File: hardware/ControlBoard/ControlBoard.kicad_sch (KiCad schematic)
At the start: 140 parts, among them J1 Lamp 1 Out, J10 CAN, J11 USB_B_Micro, J12 Conn_01x02, J13 AVAILABLE GPIO, J14 MOTOR_CTRL1, J15 MOTOR_CTRL2, J2 ESTOP1, J3 ESTOP2, J4 Lamp 3 Out, J5 Lamp 2 Out, J6 Lamp 4 Out, J7 PWR_IN, J8 USB_B_Micro, J9 UART BACKUP, Q1 2N7002, Q2 2N7002, Q3 2N7002, Q4 2N7002, Q5 SS8050-G, Q6 SS8050-G, SW1 SW_Push, SW2 SW_Push, U1 CP2102N-A02-GQFN28, U10 TXB0106PWR, U2 Lora_Module, U3 AZ1117IH-5.0TRG1, U4 LD1086DT33TR, U5 ESP32-S3-WROOM-1U, U6 74LVC1G97W6-7, U7 SN65HVD232, U8 SN74LVC1GU04DBVR, U9 TXB0106PWR

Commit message: Motor control stuff
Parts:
- R54, R55: value 1.3k -> 680
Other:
- note added: "MOTOR CONTROLLER LOW VOLTAGE = 0-0.5V, HIGH VOLTAGE = 4-5V MECH SAYS MOTOR SHAFT AT 940 RPM FOR 5 MPH 940 RPM -> 3133 HZ DRIVING SIGNAL AT 200 PULSES/REV FILTER IS JUST UNDER 0.5V / JUST OVER 4.5V IDEA IS THAT IT WILL STOP SIGNAL FROM CROSSING THRESHOLD ONCE FREQ GETS TO HIGH TO PREVENT MOTORS FROM BEING DRIVEN TOO FAST THIS IS MY ATTEMPT AT HARDWARE SPEED CONTROL CAN TINKER WITH THIS ONCE WE GET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"
- note added: "REVIEW V0.02"
- note removed: "REVIEW V0.01"
- moved on the sheet: C22, C23, C24, C25, C28, C29, R32, R33, R52, R53, R54, R55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

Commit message: Control Board Routing Work
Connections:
- net ALM+_2 is gone; now on net ALM+_2_5V: J15.9 (Pin_9), R37.1
- net DIR-_2 is gone; now on net DIR-_2_5V: R41.2
- net ENA-_2 is gone; now on net ENA-_2_5V: J15.6 (Pin_6)
- net INP+_2 is gone; now on net INP+_2_5V: J15.7 (Pin_7), R43.1
- net PUL-_2 is gone; now on net PUL-_2_5V: R40.2
- net ALM+_2_3V3: now also U10.7 (A6); no longer U10.3 (A2)
- net ALM+_2_5V: now also U10.10 (B6); no longer U10.14 (B2)
- net DIR-_2_3V3: now also U10.4 (A3); no longer U10.6 (A5)
- net DIR-_2_5V: now also U10.13 (B3); no longer U10.11 (B5)
- net INP+_2_3V3: now also U10.6 (A5); no longer U10.4 (A3)
- net INP+_2_5V: now also U10.11 (B5); no longer U10.13 (B3)
- net PUL-_2_3V3: now also U10.3 (A2); no longer U10.7 (A6)
- net PUL-_2_5V_UF: now also U10.14 (B2); no longer U10.10 (B6)
- net DIR+_2 renamed DIR+_2_5V

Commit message: JLCPCB Part #'s added and footprints verified
Checked footprints of LDOs and ICs on the board with data sheets
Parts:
- C1, C6: LCSC (none) -> C91186
- C10, C17, C18, C2, C4, C5, C8: LCSC (none) -> C92606
- C11, C12: LCSC (none) -> C1854129
- C13: LCSC (none) -> C128856
- C14, C15, C16, C19, C20, C21, C22, C23, C24, C25, C27, C28, C29, C7, C9: LCSC (none) -> C651000
- C3: LCSC (none) -> C90313
- D1, D10, D4, D6, D7, D8: LCSC (none) -> C908199
- D2, D3: LCSC (none) -> C160478
- D5, D9: LCSC (none) -> C5224083
- Q1, Q2, Q3, Q4: LCSC (none) -> C306856
- Q5, Q6: LCSC (none) -> C164886
- R1, R2, R3, R6, R7: LCSC (none) -> C280013
- R10, R14, R15, R20, R21, R22, R23, R24, R25, R26, R27, R28, R29, R30, R31, R32, R33, R34, R35, R38, R39, R40, R41, R51, R75, R76, R9: LCSC (none) -> C96345
- R12, R13, R18, R52, R53: LCSC (none) -> C110775
- R36, R37, R42, R43, R49: LCSC (none) -> C140869
- R4: LCSC (none) -> C228640
- R46, R47: LCSC (none) -> C229189
- R48: LCSC (none) -> C269726
- R5: LCSC (none) -> C137519
- R54, R55: LCSC (none) -> C229239
- R8: LCSC (none) -> C110774
- U1: LCSC (none) -> C964632
- U10, U9: LCSC (none) -> C38253
- U3: LCSC (none) -> C108496
- U4: LCSC (none) -> C12051
- U5: LCSC (none) -> C3013946
- U7: LCSC (none) -> C30530
- U8: LCSC (none) -> C81934

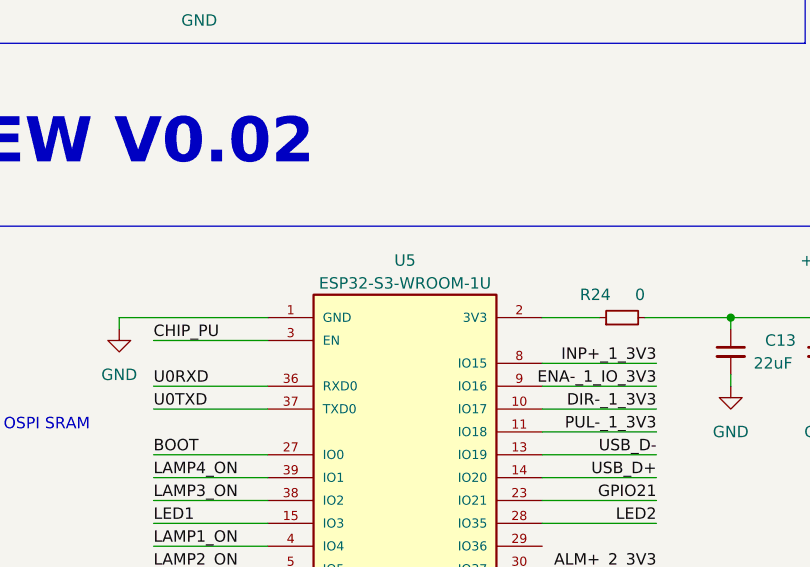
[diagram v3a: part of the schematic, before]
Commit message: Fix ESP Part Number
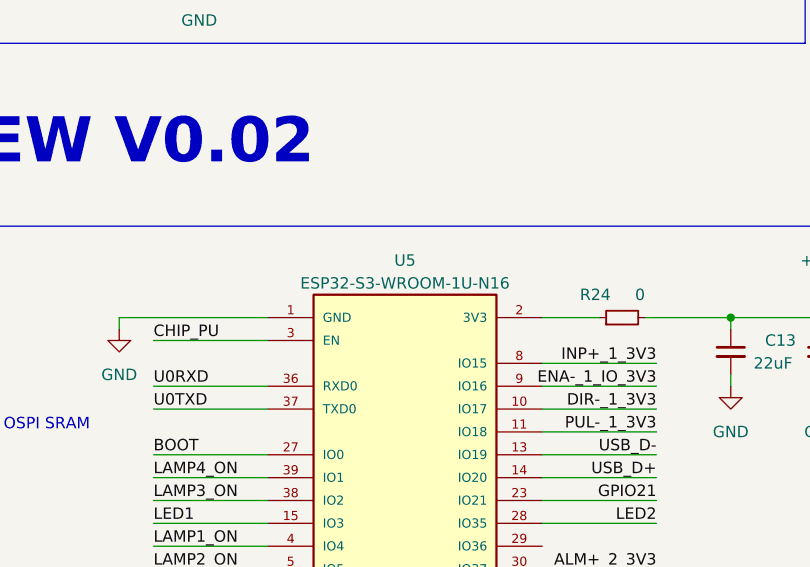
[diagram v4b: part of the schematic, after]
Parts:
- U5: value ESP32-S3-WROOM-1U -> ESP32-S3-WROOM-1U-N16; LCSC C3013946 -> C2980298
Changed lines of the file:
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@@
     (in_bom yes) (on_board yes)
     (property "Reference" "U5" (id 0) (at 242.57 154.94 0))
-    (property "Value" "ESP32-S3-WROOM-1U" (id 1) (at 242.57 157.48 0))
+    (property "Value" "ESP32-S3-WROOM-1U-N16" (id 1) (at 242.57 157.48 0))
     (property "Footprint" "XCVR_ESP32-S3-WROOM-1U" (id 2) (at 242.57 189.23 0)
       (effects (font (size 1.27 1.27)) (justify bottom) hide)
@@
       (effects (font (size 1.27 1.27)) (justify bottom) hide)
     )
-    (property "LCSC" "C3013946" (id 8) (at 242.57 189.23 0)
+    (property "LCSC" "C2980298" (id 8) (at 242.57 189.23 0)
       (effects (font (size 1.27 1.27)) hide)
     )
@@
     )
     (path "/70e03c1b-072d-443f-a14b-df670de7d8b4"
-      (reference "U5") (unit 1) (value "ESP32-S3-WROOM-1U") (footprint "XCVR_ESP32-S3-WROOM-1U")
+      (reference "U5") (unit 1) (value "ESP32-S3-WROOM-1U-N16") (footprint "XCVR_ESP32-S3-WROOM-1U")
     )
     (path "/75856a65-d647-4903-9e3e-3e5f5941022c"

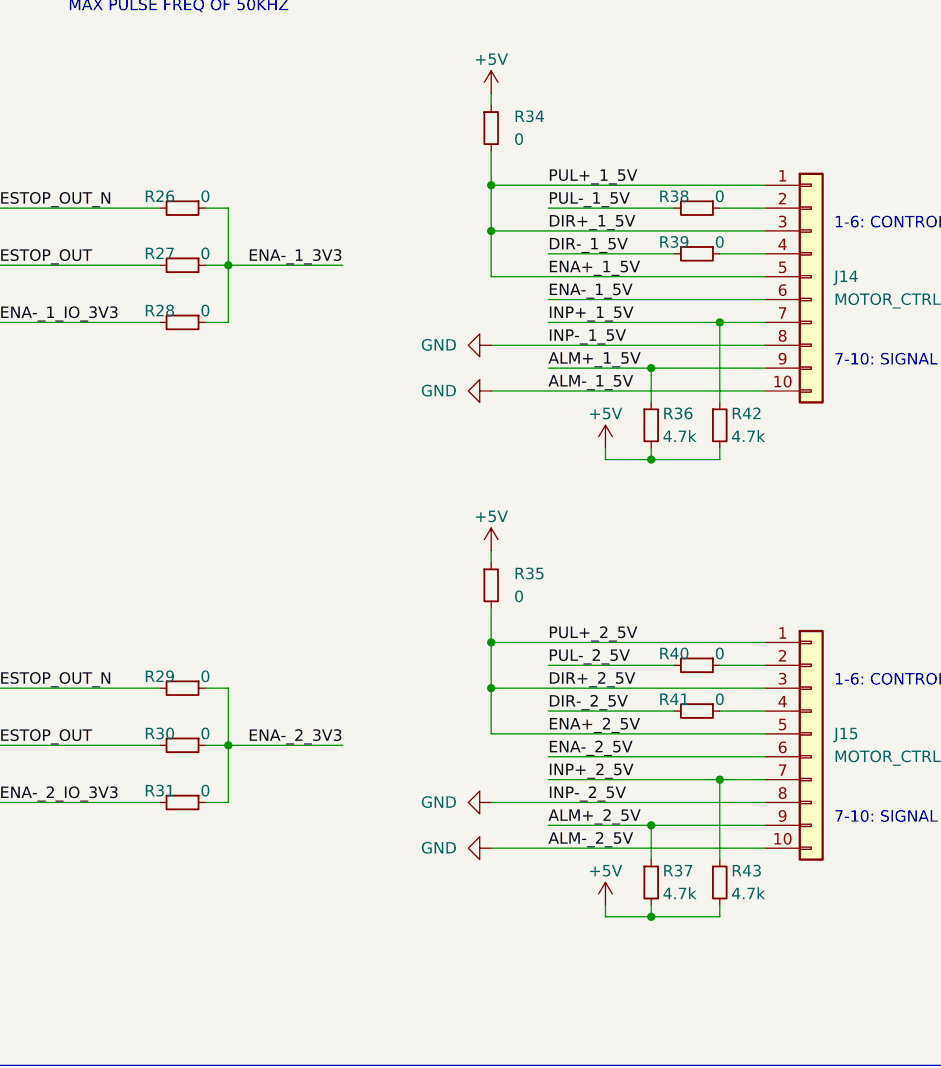
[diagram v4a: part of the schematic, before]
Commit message: Fix Pull-ups on Level Shifters
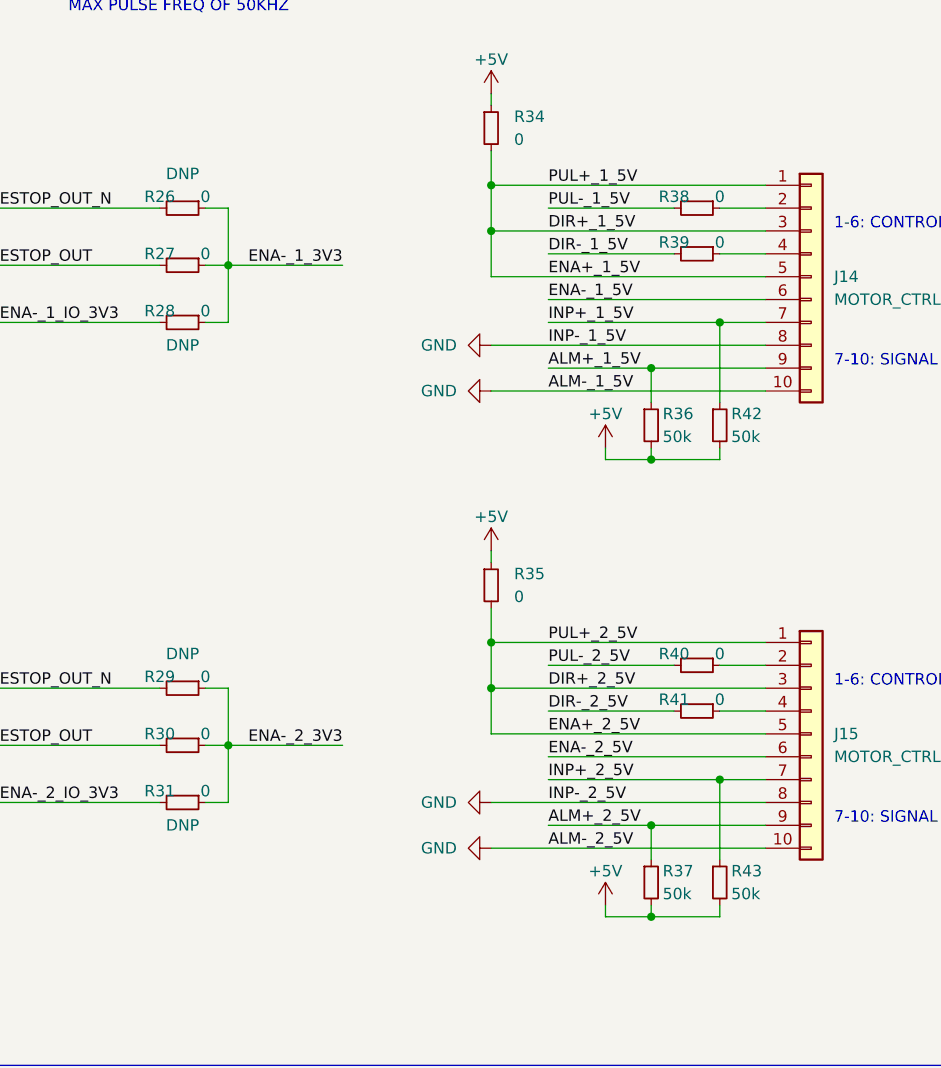
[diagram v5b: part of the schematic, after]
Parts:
- R26, R28, R29, R31: DNP (none) -> DNP
- R36, R37, R42, R43: value 4.7k -> 50k; LCSC C140869 -> C316211
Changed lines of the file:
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@@
       (effects (font (size 1.27 1.27)) hide)
     )
+    (property "DNP" "DNP" (id 5) (at 316.23 101.6 90))
     (pin "1")
     (pin "2")
@@
       (effects (font (size 1.27 1.27)) (justify left))
     )
-    (property "Value" "4.7k" (id 1) (at 377.19 128.27 0)
+    (property "Value" "50k" (id 1) (at 377.19 128.27 0)
       (effects (font (size 1.27 1.27)) (justify left))
     )
@@
       (effects (font (size 1.27 1.27)) hide)
     )
-    (property "LCSC" "C140869" (id 4) (at 375.92 127 0)
+    (property "LCSC" "C316211" (id 4) (at 375.92 127 0)
       (effects (font (size 1.27 1.27)) hide)
     )
@@
       (effects (font (size 1.27 1.27)) (justify left))
     )
-    (property "Value" "4.7k" (id 1) (at 369.57 77.47 0)
+    (property "Value" "50k" (id 1) (at 369.57 77.47 0)
       (effects (font (size 1.27 1.27)) (justify left))
     )
@@
       (effects (font (size 1.27 1.27)) hide)
     )
-    (property "LCSC" "C140869" (id 4) (at 368.3 76.2 0)
+    (property "LCSC" "C316211" (id 4) (at 368.3 76.2 0)
       (effects (font (size 1.27 1.27)) hide)
     )
@@
       (effects (font (size 1.27 1.27)) hide)
     )
+    (property "DNP" "DNP" (id 5) (at 316.23 67.31 90))
     (pin "1")
     (pin "2")
@@
       (effects (font (size 1.27 1.27)) hide)
     )
+    (property "DNP" "DNP" (id 5) (at 316.23 48.26 90))
     (pin "1")
     (pin "2")
@@
       (effects (font (size 1.27 1.27)) (justify left))
     )
-    (property "Value" "4.7k" (id 1) (at 377.19 77.47 0)
+    (property "Value" "50k" (id 1) (at 377.19 77.47 0)
       (effects (font (size 1.27 1.27)) (justify left))
     )
@@
       (effects (font (size 1.27 1.27)) hide)
     )
-    (property "LCSC" "C140869" (id 4) (at 375.92 76.2 0)
+    (property "LCSC" "C316211" (id 4) (at 375.92 76.2 0)
       (effects (font (size 1.27 1.27)) hide)
     )
@@
       (effects (font (size 1.27 1.27)) hide)
     )
+    (property "DNP" "DNP" (id 5) (at 316.23 120.65 90))
     (pin "1")
     (pin "2")
@@
       (effects (font (size 1.27 1.27)) (justify left))
     )
-    (property "Value" "4.7k" (id 1) (at 369.57 128.27 0)
+    (property "Value" "50k" (id 1) (at 369.57 128.27 0)
       (effects (font (size 1.27 1.27)) (justify left))
     )
@@
       (effects (font (size 1.27 1.27)) hide)
     )
-    (property "LCSC" "C140869" (id 4) (at 368.3 127 0)
+    (property "LCSC" "C316211" (id 4) (at 368.3 127 0)
       (effects (font (size 1.27 1.27)) hide)
     )
@@
     )
     (path "/461704da-922d-4050-833a-edfc6b9b1431"
-      (reference "R36") (unit 1) (value "4.7k") (footprint "Resistor_SMD:R_0805_2012Metric")
+      (reference "R36") (unit 1) (value "50k") (footprint "Resistor_SMD:R_0805_2012Metric")
     )
     (path "/ec9173d0-37ef-47f2-aee6-a9acb3ec61f2"
-      (reference "R37") (unit 1) (value "4.7k") (footprint "Resistor_SMD:R_0805_2012Metric")
+      (reference "R37") (unit 1) (value "50k") (footprint "Resistor_SMD:R_0805_2012Metric")
     )
     (path "/d9cac4c3-26e0-450b-9034-e41c22feeaaa"
@@
     )
     (path "/d96d2f55-7cc8-41f5-baf4-8065683b0189"
-      (reference "R42") (unit 1) (value "4.7k") (footprint "Resistor_SMD:R_0805_2012Metric")
+      (reference "R42") (unit 1) (value "50k") (footprint "Resistor_SMD:R_0805_2012Metric")
     )
     (path "/2de22fe0-cd31-4a90-a61a-d5800ab663a8"
-      (reference "R43") (unit 1) (value "4.7k") (footprint "Resistor_SMD:R_0805_2012Metric")
+      (reference "R43") (unit 1) (value "50k") (footprint "Resistor_SMD:R_0805_2012Metric")
     )
     (path "/0f03b8b2-733c-4a2d-aebd-368e5c5875d7"

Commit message: Start Review Fixes
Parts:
- removed U9: TXB0106PWR, controlLib:TXB0106PWR, symbol controlLib:TXB0106PWR
- added U?: TXB0104PW, Package_SO:TSSOP-14_4.4x5mm_P0.65mm, symbol Logic_LevelTranslator:TXB0104PW
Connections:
- net +3V3: now also U?.1 (VCCA)
- net +5V: now also U?.14 (VCCB)
- net DIR-_1_3V3: now also U?.4 (A3)
- net DIR-_1_5V: now also U?.11 (B3)
- net ENA-_1_3V3: now also U?.5 (A4)
- net ENA-_1_5V: now also U?.10 (B4)
- net GND: now also U?.7 (GND)
- net PUL-_1_3V3: now also U?.3 (A2)
- net PUL-_1_5V_UF: now also U?.12 (B2)
- net at R33.1, R53.1: now also U?.8 (OE)
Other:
- moved on the sheet: C22, C23, R33, R53

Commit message: Schematic Fixes: IO Translators, Safety Light FETs
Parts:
- removed C24, C25: 0.1u, Capacitor_SMD:C_0805_2012Metric, symbol Device:C_Small
- removed R32: 0, Resistor_SMD:R_0805_2012Metric, symbol Device:R_Small
- removed R52: 10k, Resistor_SMD:R_0805_2012Metric, symbol Device:R_Small
- removed U10: TXB0106PWR, controlLib:TXB0106PWR, symbol controlLib:TXB0106PWR
- removed U?: TXB0104PW, Package_SO:TSSOP-14_4.4x5mm_P0.65mm, symbol Logic_LevelTranslator:TXB0104PW
- added C? (x4): 0.1u, Capacitor_SMD:C_0805_2012Metric, symbol Device:C_Small
- added C? (x2): 0.1u, symbol Device:C_Small
- added C? (x6): 1u, Capacitor_SMD:C_0805_2012Metric, symbol Device:C_Small
- added R? (x8): 0, Resistor_SMD:R_0805_2012Metric, symbol Device:R_Small
- added R? (x2): 10k, Resistor_SMD:R_0805_2012Metric, symbol Device:R_Small
- added U? (x3): TXU0104QPWRQ1, controlLib:TXU0104QPWRQ1, symbol controlLib:TXU0104QPWRQ1
- added U? (x2): 74LVC1G17W5-7, controlLib:74LVC1G17W5-7, symbol controlLib:74LVC1G17W5-7
- C22: LCSC C651000 -> (none); Voltage (none) -> 3.3V
- C23, C28, C29: LCSC C651000 -> (none); Voltage (none) -> 5V
- Q1, Q2, Q3, Q4: value 2N7002 -> DMN62D0U-13; footprint Package_TO_SOT_SMD:SOT-23 -> controlLib:DMN62D0U-13; Digikey 2N7002A-7DICT-ND -> DMN62D0U-13DICT-ND; LCSC C306856 -> C156342
- R36, R37, R42, R43: value 50k -> 1k
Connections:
- net +3V3: now also R36.2, R37.2, R42.2, R43.2, C?.1, C?.1, C?.1, C?.1, C?.1, U?.1 (VCCA), U?.1 (VCCA), U?.1 (VCCA)
- net +5V: now also C?.1, C?.1, C?.1, C?.1, C?.1, C?.2, C?.2, U?.14 (VCCB), U?.14 (VCCB), U?.14 (VCCB), U?.5 (VCC), U?.5 (VCC); no longer R36.2, R37.2, R42.2, R43.2
- net DIR-_1_3V3: now also U?.4 (A3), U?.4 (A3)
- net DIR-_1_5V: now also U?.11 (B3Y), U?.11 (B3Y)
- net DIR-_2_3V3: now also U?.4 (A3)
- net DIR-_2_5V: now also U?.11 (B3Y)
- net ENA-_1_3V3: now also U?.5 (A4), U?.5 (A4)
- net ENA-_1_5V: now also U?.10 (B4Y), U?.10 (B4Y)
- net ENA-_2_3V3: now also U?.5 (A4)
- net ENA-_2_5V: now also U?.10 (B4Y)
- net ESTOP_OUT_N: now also R?.2, R?.2
- net GND: now also C?.1, C?.1, C?.2, C?.2, C?.2, C?.2, C?.2, C?.2, C?.2, C?.2, C?.2, C?.2, R?.1, R?.1, R?.1, R?.2, R?.2, R?.2, R?.2, R?.2, U?.3 (GND), U?.3 (GND), U?.7 (GND), U?.7 (GND), U?.7 (GND)
- net PUL-_1_3V3: now also U?.3 (A2), U?.3 (A2)
- net PUL-_1_5V: now also U?.4 (Y); no longer C29.1, R55.2
- net PUL-_1_5V_UF: now also U?.12 (B2Y), U?.12 (B2Y)
- net PUL-_2_3V3: now also U?.3 (A2)
- net PUL-_2_5V: now also U?.4 (Y); no longer C28.1, R54.2
- net PUL-_2_5V_UF: now also U?.12 (B2Y)
- net at R33.1, R53.1: now also U?.8 (OE)
- new net: R?.1, U?.13 (B1Y) (x3)
- new net: R?.2, U?.2 (A1) (x3)
- new net: R?.1, R?.1, U?.8 (OE) (x2)
- new net: C28.1, R54.2, U?.2 (A)
- new net: C29.1, R55.2, U?.2 (A)
- no-connect marks 17 -> 25
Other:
- note added: "Buffer min high output voltage is 3.8V @ VCC=4.5V Buffer max low output voltage is 0.55V @ VCC=4.5V Could not find a part with voltages closer to 0/5V These extremes are a bit under/over limits for high/low on controller but Vcc=5V is higher than Vcc=4.5V I'm thinking we can take the risk, worst case we give up on the speed control filter To remove, solder bridge A and Y pins of buffer, remove fi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"
- note added: "FET PN: DMN62D0U-13"
- moved on the sheet: C22, C23, C28, C29, R33, R53, R54, R55

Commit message: Fixing the things
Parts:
- removed C22, C23: 0.1u, Capacitor_SMD:C_0805_2012Metric, symbol Device:C_Small
- removed C? (x2): 1u, Capacitor_SMD:C_0805_2012Metric, symbol Device:C_Small
- removed R33, R? (x2): 0, Resistor_SMD:R_0805_2012Metric, symbol Device:R_Small
- removed R53: 10k, Resistor_SMD:R_0805_2012Metric, symbol Device:R_Small
- removed U?: TXU0104QPWRQ1, controlLib:TXU0104QPWRQ1, symbol controlLib:TXU0104QPWRQ1
- added C? (x4): 0.1u, Capacitor_SMD:C_0805_2012Metric, symbol Device:C_Small
- added R?: 0, Resistor_SMD:R_0805_2012Metric, symbol Device:R_Small
- C11: LCSC C1854129 -> (none); Voltage (none) -> 3.3V
- C15, C16: value 0.1uF -> 0.1u; DNP (none) -> DNP; LCSC C651000 -> (none); Voltage (none) -> 3.3V
- C18: LCSC C92606 -> (none); Voltage (none) -> 3.3V
- C4, C8: Voltage (none) -> 12V
- C5: LCSC C92606 -> (none); Voltage (none) -> 5V
- J11, J8: footprint Connector_USB:USB_Micro-B_Molex-105017-0001 -> Connector_USB:USB_Micro-B_Amphenol_10118194_Horizontal; Digikey WM1399CT-ND -> 609-4618-1-ND; LCSC (none) -> C132563
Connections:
- net ALM+_1_5V is gone; now on net ALM+_1_3V3: J14.9 (Pin_9), R36.1
- net ALM+_2_5V is gone; now on net ALM+_2_3V3: J15.9 (Pin_9), R37.1
- net INP+_1_5V is gone; now on net INP+_1_3V3: J14.7 (Pin_7), R42.1
- net INP+_2_5V is gone; now on net INP+_2_3V3: J15.7 (Pin_7), R43.1
- net +12V: now also C?.2, C?.2
- net +3V3: now also C?.1
- net +5V: now also C?.2
- net ESTOP_OUT: now also R?.2; no longer U5.16 (IO46)
- net GND: now also C?.1, C?.1, C?.1, C?.2
- new net: R?.1, U5.16 (IO46)
- no-connect marks 25 -> 23
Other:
- note added: "Buffer min high output voltage is 3.8V @ VCC=4.5V Buffer max low output voltage is 0.55V @ VCC=4.5V Could not find a part with voltages closer to 0/5V These extremes are a bit under/over limits for high/low on controller but Vcc=5V is higher than Vcc=4.5V I'm thinking we can take the risk, worst case we give up on the speed control filter To remove, depop buffer and bridge A and Y pins, remove fi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"
- note added: "GPIO 46 NEEDS TO BE LOW TO ENABLE PROGRAMMING 0 OHM IN CASE ESTOP_OUT MESSES UP INTERNAL PULL DOWN (I DON'T THINK IT SHOULD IF ESTOP ISN'T ACTIVE?)"
- note removed: "Buffer min high output voltage is 3.8V @ VCC=4.5V Buffer max low output voltage is 0.55V @ VCC=4.5V Could not find a part with voltages closer to 0/5V These extremes are a bit under/over limits for high/low on controller but Vcc=5V is higher than Vcc=4.5V I'm thinking we can take the risk, worst case we give up on the speed control filter To remove, solder bridge A and Y pins of buffer, remove fi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"
- moved on the sheet: C15, C16, C18, C4, C5, C8, SW1, SW2, TP2, TP3
